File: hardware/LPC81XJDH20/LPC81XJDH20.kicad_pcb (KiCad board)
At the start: 2 copper layers, 18.7 x 26.2 mm, 20 parts, among them J1 LPC81XJDH20_breakout_left, J2 JTAG_2X05, J3 LPC81XJDH20_breakout_right, U3 LPC812M101JDH20, Y1 12MHz

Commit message: various beauty changes
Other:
- board size 18.7 x 26.2 mm -> 18.6 x 26.2 mm
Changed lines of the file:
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@@
     (46 B.CrtYd user)
     (47 F.CrtYd user)
-    (48 B.Fab user hide)
-    (49 F.Fab user hide)
+    (48 B.Fab user)
+    (49 F.Fab user)
   )
   (setup
-    (last_trace_width 0.4)
+    (last_trace_width 0.1524)
     (user_trace_width 0.1524)
     (user_trace_width 0.2)
@@
       (effects (font (size 1 1) (thickness 0.15)) (justify left bottom))
     )
-    (fp_text value LPC812M101JDH20 (at 4.6 3.1 270) (layer F.Fab)
+    (fp_text value LPC812M101JDH20 (at 4.6 3.1 270) (layer F.Fab) hide
       (effects (font (size 1 1) (thickness 0.15)) (justify left bottom))
     )
@@
       (effects (font (size 1 1) (thickness 0.15)) (justify mirror))
     )
-    (fp_text value LPC81XJDH20_breakout_left (at 0 -2.1 270) (layer B.Fab)
+    (fp_text value LPC81XJDH20_breakout_left (at 0 -2.1 270) (layer B.Fab) hide
       (effects (font (size 1 1) (thickness 0.15)) (justify mirror))
     )
@@
       (effects (font (size 1 1) (thickness 0.15)) (justify mirror))
     )
-    (fp_text value LPC81XJDH20_breakout_right (at 0 -2.1 270) (layer B.Fab)
+    (fp_text value LPC81XJDH20_breakout_right (at 0 -2.1 270) (layer B.Fab) hide
       (effects (font (size 1 1) (thickness 0.15)) (justify mirror))
     )
@@
   )
   (gr_line (start 125.3 114.7) (end 125.3 88.5) (layer Edge.Cuts) (width 0.2))
-  (gr_line (start 144 114.7) (end 125.3 114.7) (layer Edge.Cuts) (width 0.2))
-  (gr_line (start 143.9 88.5) (end 144 114.7) (layer Edge.Cuts) (width 0.2))
+  (gr_line (start 143.9 114.7) (end 125.3 114.7) (layer Edge.Cuts) (width 0.2))
+  (gr_line (start 143.9 88.5) (end 143.9 114.7) (layer Edge.Cuts) (width 0.2))
   (gr_line (start 125.3 88.5) (end 143.9 88.5) (layer Edge.Cuts) (width 0.2))
   (segment (start 139.6 92) (end 138.5 92) (width 0.6) (layer F.Cu) (net 1))
@@
   (segment (start 136.9 93.8) (end 136.9 92.45) (width 0.2) (layer F.Cu) (net 2))
   (segment (start 129.5 92.45) (end 136.9 92.45) (width 0.4) (layer B.Cu) (net 2))
-  (segment (start 136.9 92.45) (end 136.9 91.5) (width 0.4) (layer B.Cu) (net 2))
-  (segment (start 136.9 91.5) (end 137.1 91.3) (width 0.4) (layer B.Cu) (net 2))
-  (segment (start 137.1 91.3) (end 137.9 91.3) (width 0.4) (layer B.Cu) (net 2))
   (segment (start 137.9 90.3) (end 137.9 91.3) (width 0.4) (layer B.Cu) (net 2))
   (segment (start 139.6 90) (end 140.5 90) (width 0.6) (layer F.Cu) (net 2))
@@
   (segment (start 136.85 109.8) (end 140.5 109.8) (width 0.4) (layer B.Cu) (net 2))
   (segment (start 140.5 109.8) (end 140.85 109.45) (width 0.4) (layer B.Cu) (net 2))
+  (segment (start 137.4 91.3) (end 137.9 91.3) (width 0.4) (layer B.Cu) (net 2))
+  (segment (start 136.9 92.45) (end 136.9 91.8) (width 0.4) (layer B.Cu) (net 2))
+  (segment (start 136.9 91.8) (end 137.4 91.3) (width 0.4) (layer B.Cu) (net 2))
   (segment (start 128.4 108.3) (end 128.4 109.09) (width 0.2) (layer F.Cu) (net 3))
   (segment (start 129.5 107.2) (end 128.4 108.3) (width 0.2) (layer F.Cu) (net 3))
@@
   (zone (net 1) (net_name VSS) (layer B.Cu) (hatch edge 0.508)
     (connect_pads (clearance 0.3))
-    (min_thickness 0.2)
-    (fill yes (arc_segments 16) (thermal_gap 0.3) (thermal_bridge_width 0.3))
+    (min_thickness 0.3)
+    (fill yes (arc_segments 16) (thermal_gap 0.3) (thermal_bridge_width 0.4))
     (polygon
       (pts
@@
   (zone (net 1) (net_name VSS) (layer F.Cu) (hatch edge 0.508)
     (connect_pads (clearance 0.3))
-    (min_thickness 0.254)
-    (fill yes (arc_segments 16) (thermal_gap 0.3) (thermal_bridge_width 0.3))
+    (min_thickness 0.3)
+    (fill yes (arc_segments 16) (thermal_gap 0.3) (thermal_bridge_width 0.4))
     (polygon
       (pts
-        (xy 125.3 88.5) (xy 143.9 88.5) (xy 144 114.7) (xy 125.3 114.7)
+        (xy 125.3 88.5) (xy 143.9 88.5) (xy 143.9 114.7) (xy 125.3 114.7)
       )
     )

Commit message: final small changes to PCB
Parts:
- R4, R5, R6: value 100 -> 33
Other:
- board size 18.6 x 26.2 mm -> 18.4 x 26 mm
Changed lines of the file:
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@@
       (effects (font (size 1 1) (thickness 0.15)))
     )
-    (fp_text value 12MHz (at 1.3 3.45) (layer F.Fab)
+    (fp_text value 12MHz (at 1.7 2.65 90) (layer F.Fab)
       (effects (font (size 1 1) (thickness 0.15)))
     )
@@
       (effects (font (size 1 1) (thickness 0.15)))
     )
-    (fp_text value 18p (at -0.6 -1.75 180) (layer F.Fab)
+    (fp_text value 18p (at -1 1.15 180) (layer F.Fab)
       (effects (font (size 1 1) (thickness 0.15)))
     )
@@
       (effects (font (size 1 1) (thickness 0.15)))
     )
-    (fp_text value 1u (at 0.8 3 180) (layer F.Fab)
+    (fp_text value 1u (at 2.4 0.1 180) (layer F.Fab)
       (effects (font (size 1 1) (thickness 0.15)))
     )
@@
       (effects (font (size 1 1) (thickness 0.15)))
     )
-    (fp_text value 18p (at -2 -0.05) (layer F.Fab)
+    (fp_text value 18p (at 2.2 0.05) (layer F.Fab)
       (effects (font (size 1 1) (thickness 0.15)))
     )
@@
       (effects (font (size 1 1) (thickness 0.15)))
     )
-    (fp_text value 100n (at -3 0.2) (layer F.Fab)
+    (fp_text value 100n (at 2.9 0) (layer F.Fab)
       (effects (font (size 1 1) (thickness 0.15)))
     )
@@
       (effects (font (size 1 1) (thickness 0.15)))
     )
-    (fp_text value FB (at 2.3 0.05 180) (layer F.Fab)
+    (fp_text value FB (at 2.4 -0.95 270) (layer F.Fab)
       (effects (font (size 1 1) (thickness 0.15)))
     )
@@
       (effects (font (size 1 1) (thickness 0.15)))
     )
-    (fp_text value 100 (at -2.2 -0.5 180) (layer F.Fab)
+    (fp_text value 33 (at -2.2 -0.5 180) (layer F.Fab)
       (effects (font (size 1 1) (thickness 0.15)))
     )
@@
       (effects (font (size 1 1) (thickness 0.15)))
     )
-    (fp_text value 100 (at -0.5 -2.8 180) (layer F.Fab)
+    (fp_text value 33 (at -0.5 -2.8 180) (layer F.Fab)
       (effects (font (size 1 1) (thickness 0.15)))
     )
@@
       (effects (font (size 1 1) (thickness 0.15)))
     )
-    (fp_text value 100 (at -1.2 2.8 180) (layer F.Fab)
+    (fp_text value 33 (at -1.2 2.8 180) (layer F.Fab)
       (effects (font (size 1 1) (thickness 0.15)))
     )
@@
     (tags "PIN HEADER")
     (attr virtual)
-    (fp_text reference J1 (at 2.8 -2.1 270) (layer B.SilkS)
+    (fp_text reference J1 (at -12 -2.3) (layer B.SilkS)
       (effects (font (size 1 1) (thickness 0.15)) (justify mirror))
     )
@@
     (fp_line (start 10.16 -0.635) (end 10.795 -1.27) (layer B.SilkS) (width 0.1524))
     (fp_line (start 12.065 -1.27) (end 10.795 -1.27) (layer B.SilkS) (width 0.1524))
-    (fp_text user VSS (at -11 -2.3 180) (layer B.SilkS)
+    (fp_text user VSS (at -10.7 -2.3 180) (layer B.SilkS)
       (effects (font (size 0.6 0.6) (thickness 0.125)) (justify mirror))
     )
@@
       (effects (font (size 0.6 0.6) (thickness 0.15)) (justify mirror))
     )
-    (fp_text user PIO0_15 (at 4.4 -3.3 180) (layer B.SilkS)
+    (fp_text user PIO0_15 (at 4.6 -3.3 180) (layer B.SilkS)
       (effects (font (size 0.6 0.6) (thickness 0.15)) (justify mirror))
     )
@@
     (tags "PIN HEADER")
     (attr virtual)
-    (fp_text reference J3 (at 2.8 2.24 270) (layer B.SilkS)
+    (fp_text reference J3 (at -12 2.34) (layer B.SilkS)
       (effects (font (size 1 1) (thickness 0.15)) (justify mirror))
     )
@@
     (fp_line (start 10.16 -0.635) (end 10.795 -1.27) (layer B.SilkS) (width 0.1524))
     (fp_line (start 12.065 -1.27) (end 10.795 -1.27) (layer B.SilkS) (width 0.1524))
-    (fp_text user VDD (at -11.4 2.34 180) (layer B.SilkS)
+    (fp_text user VDD (at -10.5 2.44 180) (layer B.SilkS)
       (effects (font (size 0.6 0.6) (thickness 0.15)) (justify mirror))
     )
@@
       (net 2 VDD))
   )
-  (gr_line (start 125.3 114.7) (end 125.3 88.5) (layer Edge.Cuts) (width 0.2))
-  (gr_line (start 143.9 114.7) (end 125.3 114.7) (layer Edge.Cuts) (width 0.2))
-  (gr_line (start 143.9 88.5) (end 143.9 114.7) (layer Edge.Cuts) (width 0.2))
-  (gr_line (start 125.3 88.5) (end 143.9 88.5) (layer Edge.Cuts) (width 0.2))
+  (gr_line (start 125.4 114.6) (end 125.4 88.6) (layer Edge.Cuts) (width 0.2))
+  (gr_line (start 143.8 114.6) (end 125.4 114.6) (layer Edge.Cuts) (width 0.2))
+  (gr_line (start 143.8 88.6) (end 143.8 114.6) (layer Edge.Cuts) (width 0.2))
+  (gr_line (start 125.4 88.6) (end 143.8 88.6) (layer Edge.Cuts) (width 0.2))
   (segment (start 139.6 92) (end 138.5 92) (width 0.6) (layer F.Cu) (net 1))
   (via (at 138.5 92) (size 0.55) (drill 0.4) (layers F.Cu B.Cu) (net 1))
@@
   (segment (start 136.6 96.1) (end 141.39 96.1) (width 0.2) (layer F.Cu) (net 17))
   (segment (start 135.575 97.125) (end 136.6 96.1) (width 0.2) (layer F.Cu) (net 17))
-  (segment (start 140.59 97.79) (end 142.24 97.79) (width 0.2) (layer F.Cu) (net 18))
-  (segment (start 139.3 96.5) (end 140.59 97.79) (width 0.2) (layer F.Cu) (net 18))
-  (segment (start 136.8 96.5) (end 139.3 96.5) (width 0.2) (layer F.Cu) (net 18))
+  (segment (start 140.79 97.79) (end 142.24 97.79) (width 0.2) (layer F.Cu) (net 18))
+  (segment (start 136.8 96.5) (end 139.5 96.5) (width 0.2) (layer F.Cu) (net 18))
+  (segment (start 139.5 96.5) (end 140.79 97.79) (width 0.2) (layer F.Cu) (net 18))
   (segment (start 136.225 98.675) (end 136.225 97.075) (width 0.2) (layer F.Cu) (net 18))
   (segment (start 136.225 97.075) (end 136.8 96.5) (width 0.2) (layer F.Cu) (net 18))
@@
   (segment (start 136.875 98.675) (end 136.875 97.125) (width 0.2) (layer F.Cu) (net 19))
   (segment (start 136.875 97.125) (end 137.1 96.9) (width 0.2) (layer F.Cu) (net 19))
-  (segment (start 137.625 98.675) (end 137.625 97.675) (width 0.2) (layer F.Cu) (net 20))
-  (segment (start 137.625 97.675) (end 137.9 97.4) (width 0.2) (layer F.Cu) (net 20))
-  (segment (start 137.9 97.4) (end 138.6 97.4) (width 0.2) (layer F.Cu) (net 20))
-  (segment (start 138.6 97.4) (end 140.6 99.4) (width 0.2) (layer F.Cu) (net 20))
   (segment (start 140.6 101.23) (end 142.24 102.87) (width 0.2) (layer F.Cu) (net 20))
   (segment (start 140.6 99.4) (end 140.6 101.23) (width 0.2) (layer F.Cu) (net 20))
+  (segment (start 138.5 97.3) (end 140.6 99.4) (width 0.2) (layer F.Cu) (net 20))
+  (segment (start 138 97.3) (end 138.5 97.3) (width 0.2) (layer F.Cu) (net 20))
+  (segment (start 137.625 98.675) (end 137.625 97.675) (width 0.2) (layer F.Cu) (net 20))
+  (segment (start 137.625 97.675) (end 138 97.3) (width 0.2) (layer F.Cu) (net 20))
   (segment (start 137.625 104.525) (end 137.625 105.425) (width 0.2) (layer F.Cu) (net 21))
   (segment (start 137.625 105.425) (end 137.8 105.6) (width 0.2) (layer F.Cu) (net 21))
@@
   (segment (start 136.875 105.275) (end 137.7 106.1) (width 0.2) (layer F.Cu) (net 22))
   (segment (start 128.7 101.17) (end 127 102.87) (width 0.2) (layer F.Cu) (net 23))
-  (segment (start 128.7 99.3) (end 128.7 101.17) (width 0.2) (layer F.Cu) (net 23))
-  (segment (start 130.5 97.5) (end 128.7 99.3) (width 0.2) (layer F.Cu) (net 23))
-  (segment (start 131.3 97.5) (end 130.5 97.5) (width 0.2) (layer F.Cu) (net 23))
+  (segment (start 128.7 99.6) (end 128.7 101.17) (width 0.2) (layer F.Cu) (net 23))
+  (segment (start 130.8 97.5) (end 128.7 99.6) (width 0.2) (layer F.Cu) (net 23))
+  (segment (start 131.3 97.5) (end 130.8 97.5) (width 0.2) (layer F.Cu) (net 23))
   (segment (start 131.575 98.675) (end 131.575 97.775) (width 0.2) (layer F.Cu) (net 23))
   (segment (start 131.575 97.775) (end 131.3 97.5) (width 0.2) (layer F.Cu) (net 23))

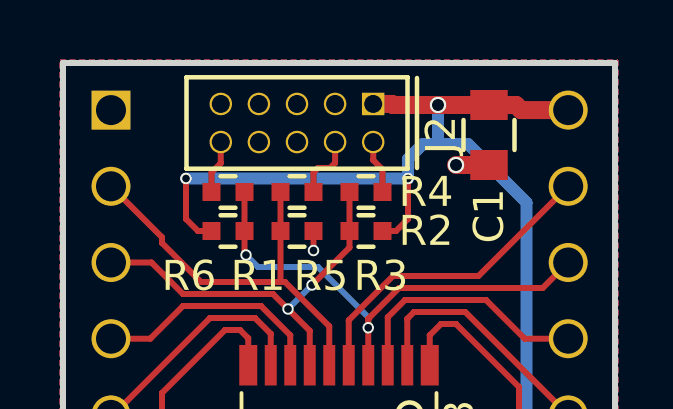
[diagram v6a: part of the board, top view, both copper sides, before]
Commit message: fixed mistake with shrunk groundplane, updated readme
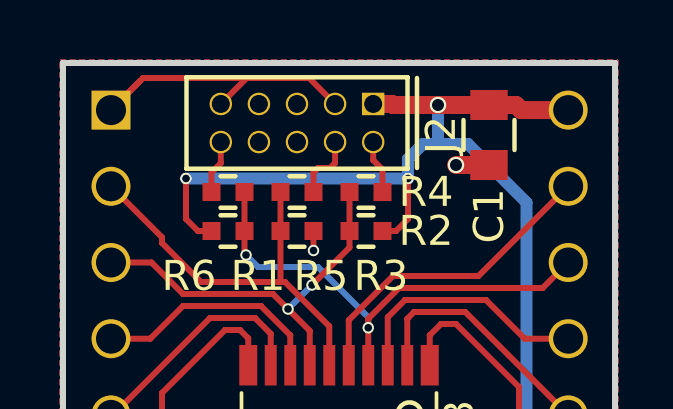
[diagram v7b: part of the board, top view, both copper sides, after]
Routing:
- net VSS: track 12.2 -> 23.1 mm
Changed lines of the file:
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@@
     (thickness 1.6)
     (drawings 4)
-    (tracks 209)
+    (tracks 214)
     (zones 0)
     (modules 20)
@@
   )
   (setup
-    (last_trace_width 0.1524)
+    (last_trace_width 0.2)
     (user_trace_width 0.1524)
     (user_trace_width 0.2)
@@
   (segment (start 135.15 105.65) (end 135.15 106.2) (width 0.4) (layer F.Cu) (net 1))
   (segment (start 134.925 105.425) (end 135.15 105.65) (width 0.4) (layer F.Cu) (net 1))
+  (segment (start 130.66 89.965) (end 131.525 89.1) (width 0.2) (layer F.Cu) (net 1))
+  (segment (start 127 90.17) (end 127.97 89.2) (width 0.2) (layer F.Cu) (net 1))
+  (segment (start 127 90.17) (end 128.07 89.1) (width 0.2) (layer F.Cu) (net 1))
+  (segment (start 133.605 89.1) (end 134.47 89.965) (width 0.2) (layer F.Cu) (net 1))
+  (segment (start 128.07 89.1) (end 133.605 89.1) (width 0.2) (layer F.Cu) (net 1))
   (segment (start 135.74 89.965) (end 136.365 89.965) (width 0.6) (layer F.Cu) (net 2))
   (segment (start 136.365 89.965) (end 136.4 90) (width 0.6) (layer F.Cu) (net 2))

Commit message: newer LPC812 schematic component, changed paste vs pad
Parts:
- N2: value 20190310 -> 20190313
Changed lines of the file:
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@@
     (37 F.SilkS user)
     (38 B.Mask user)
-    (39 F.Mask user)
+    (39 F.Mask user hide)
     (40 Dwgs.User user)
     (41 Cmts.User user)
@@
   )
   (setup
-    (last_trace_width 0.2)
+    (last_trace_width 0.1524)
     (user_trace_width 0.1524)
     (user_trace_width 0.2)
@@
     (pad_to_mask_clearance 0.1)
     (solder_mask_min_width 0.25)
+    (pad_to_paste_clearance_ratio -0.1)
     (aux_axis_origin 0 0)
     (visible_elements FFFFFF7F)
@@
       (effects (font (size 1 1) (thickness 0.15)) (justify mirror))
     )
-    (fp_text value 20190310 (at -0.4 0.1) (layer B.SilkS)
+    (fp_text value 20190313 (at -0.4 0.1) (layer B.SilkS)
       (effects (font (size 1 1) (thickness 0.15)) (justify mirror))
     )
